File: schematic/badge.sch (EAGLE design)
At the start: 13 parts, among them IC1 4051D, IC2 4051D

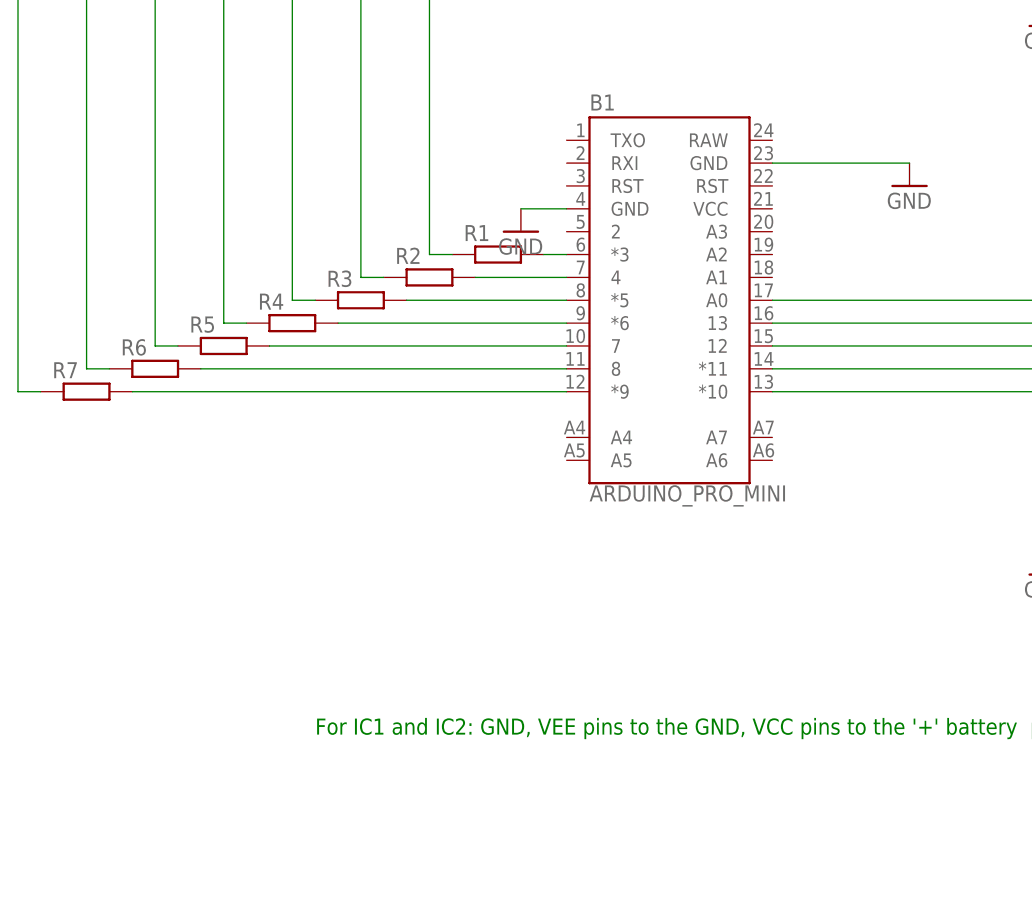
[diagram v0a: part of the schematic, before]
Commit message: Added schematic
This is first version of the schematic which I used for testing idea and
program. Now I work for the new design
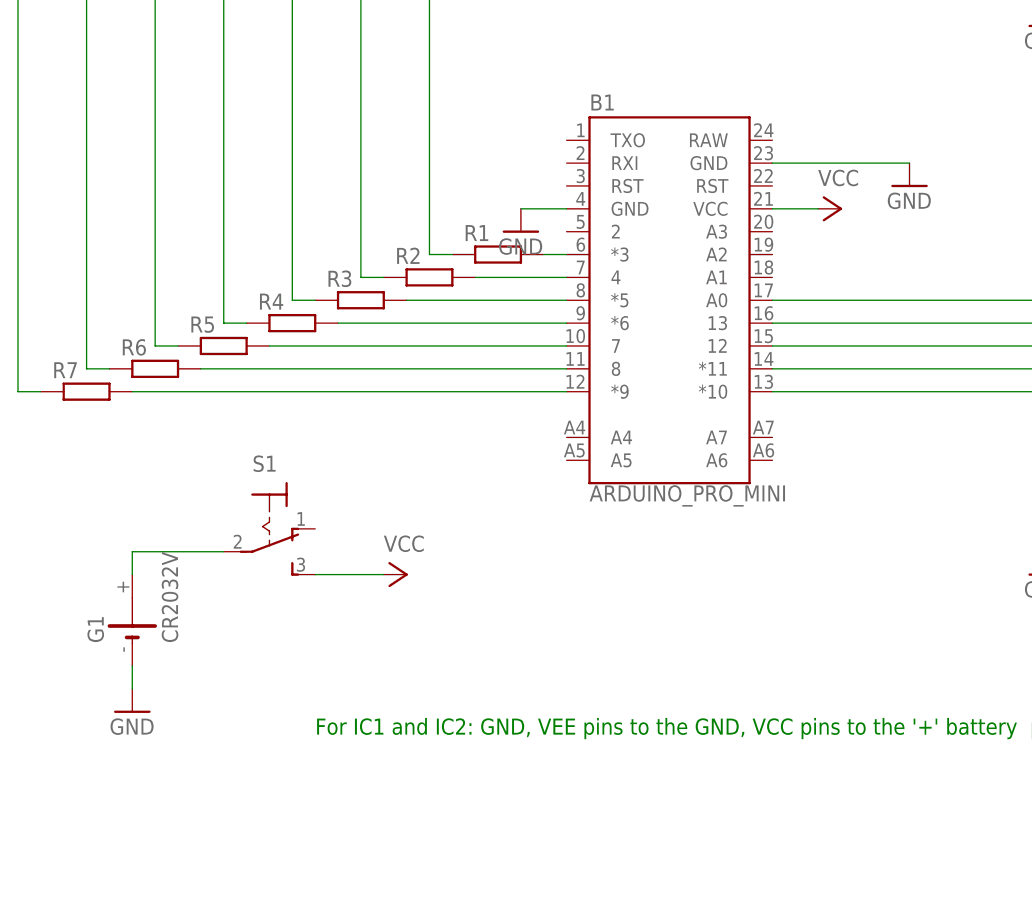
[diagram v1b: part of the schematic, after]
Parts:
- added G1: CR2032V, battery:CR2032V
- added S1: (no value), switch:320-916
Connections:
- new net N$33: G1.+, S1.P
- new net VCC: B1.VCC, S1.S
- net GND: now also G1.-
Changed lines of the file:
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@@
 <part name="GND3" library="supply1" library_urn="urn:adsk.eagle:library:371" deviceset="GND" device=""/>
 <part name="GND4" library="supply1" library_urn="urn:adsk.eagle:library:371" deviceset="GND" device=""/>
+<part name="G1" library="battery" library_urn="urn:adsk.eagle:library:109" deviceset="CR2032V" device="" package3d_urn="urn:adsk.eagle:package:4578/1"/>
+<part name="S1" library="switch" library_urn="urn:adsk.eagle:library:380" deviceset="320-916" device="" package3d_urn="urn:adsk.eagle:package:27678/1"/>
+<part name="P+1" library="supply1" library_urn="urn:adsk.eagle:library:371" deviceset="VCC" device=""/>
+<part name="P+2" library="supply1" library_urn="urn:adsk.eagle:library:371" deviceset="VCC" device=""/>
+<part name="GND5" library="supply1" library_urn="urn:adsk.eagle:library:371" deviceset="GND" device=""/>
 </parts>
 <sheets>
@@
 <instance part="GND3" gate="1" x="15.24" y="43.18"/>
 <instance part="GND4" gate="1" x="-27.94" y="38.1"/>
+<instance part="G1" gate="1" x="-71.12" y="-5.08" rot="R90"/>
+<instance part="S1" gate="1" x="-55.88" y="5.08" rot="R270"/>
+<instance part="P+1" gate="VCC" x="-40.64" y="0" rot="R270"/>
+<instance part="P+2" gate="VCC" x="7.62" y="40.64" rot="R270"/>
+<instance part="GND5" gate="1" x="-71.12" y="-15.24"/>
 </instances>
 <busses>
@@
 <wire x1="-27.94" y1="40.64" x2="-22.86" y2="40.64" width="0.1524" layer="91"/>
 </segment>
+<segment>
+<pinref part="GND5" gate="1" pin="GND"/>
+<pinref part="G1" gate="1" pin="-"/>
+<wire x1="-71.12" y1="-12.7" x2="-71.12" y2="-10.16" width="0.1524" layer="91"/>
+</segment>
 </net>
 <net name="N$8" class="0">
@@
 </segment>
 </net>
+<net name="VCC" class="0">
+<segment>
+<pinref part="P+2" gate="VCC" pin="VCC"/>
+<pinref part="B1" gate="G$1" pin="VCC"/>
+<wire x1="5.08" y1="40.64" x2="0" y2="40.64" width="0.1524" layer="91"/>
+</segment>
+<segment>
+<pinref part="P+1" gate="VCC" pin="VCC"/>
+<pinref part="S1" gate="1" pin="S"/>
+<wire x1="-43.18" y1="0" x2="-50.8" y2="0" width="0.1524" layer="91"/>
+</segment>
+</net>
+<net name="N$33" class="0">
+<segment>
+<pinref part="S1" gate="1" pin="P"/>
+<wire x1="-60.96" y1="2.54" x2="-71.12" y2="2.54" width="0.1524" layer="91"/>
+<pinref part="G1" gate="1" pin="+"/>
+<wire x1="-71.12" y1="2.54" x2="-71.12" y2="0" width="0.1524" layer="91"/>
+</segment>
+</net>

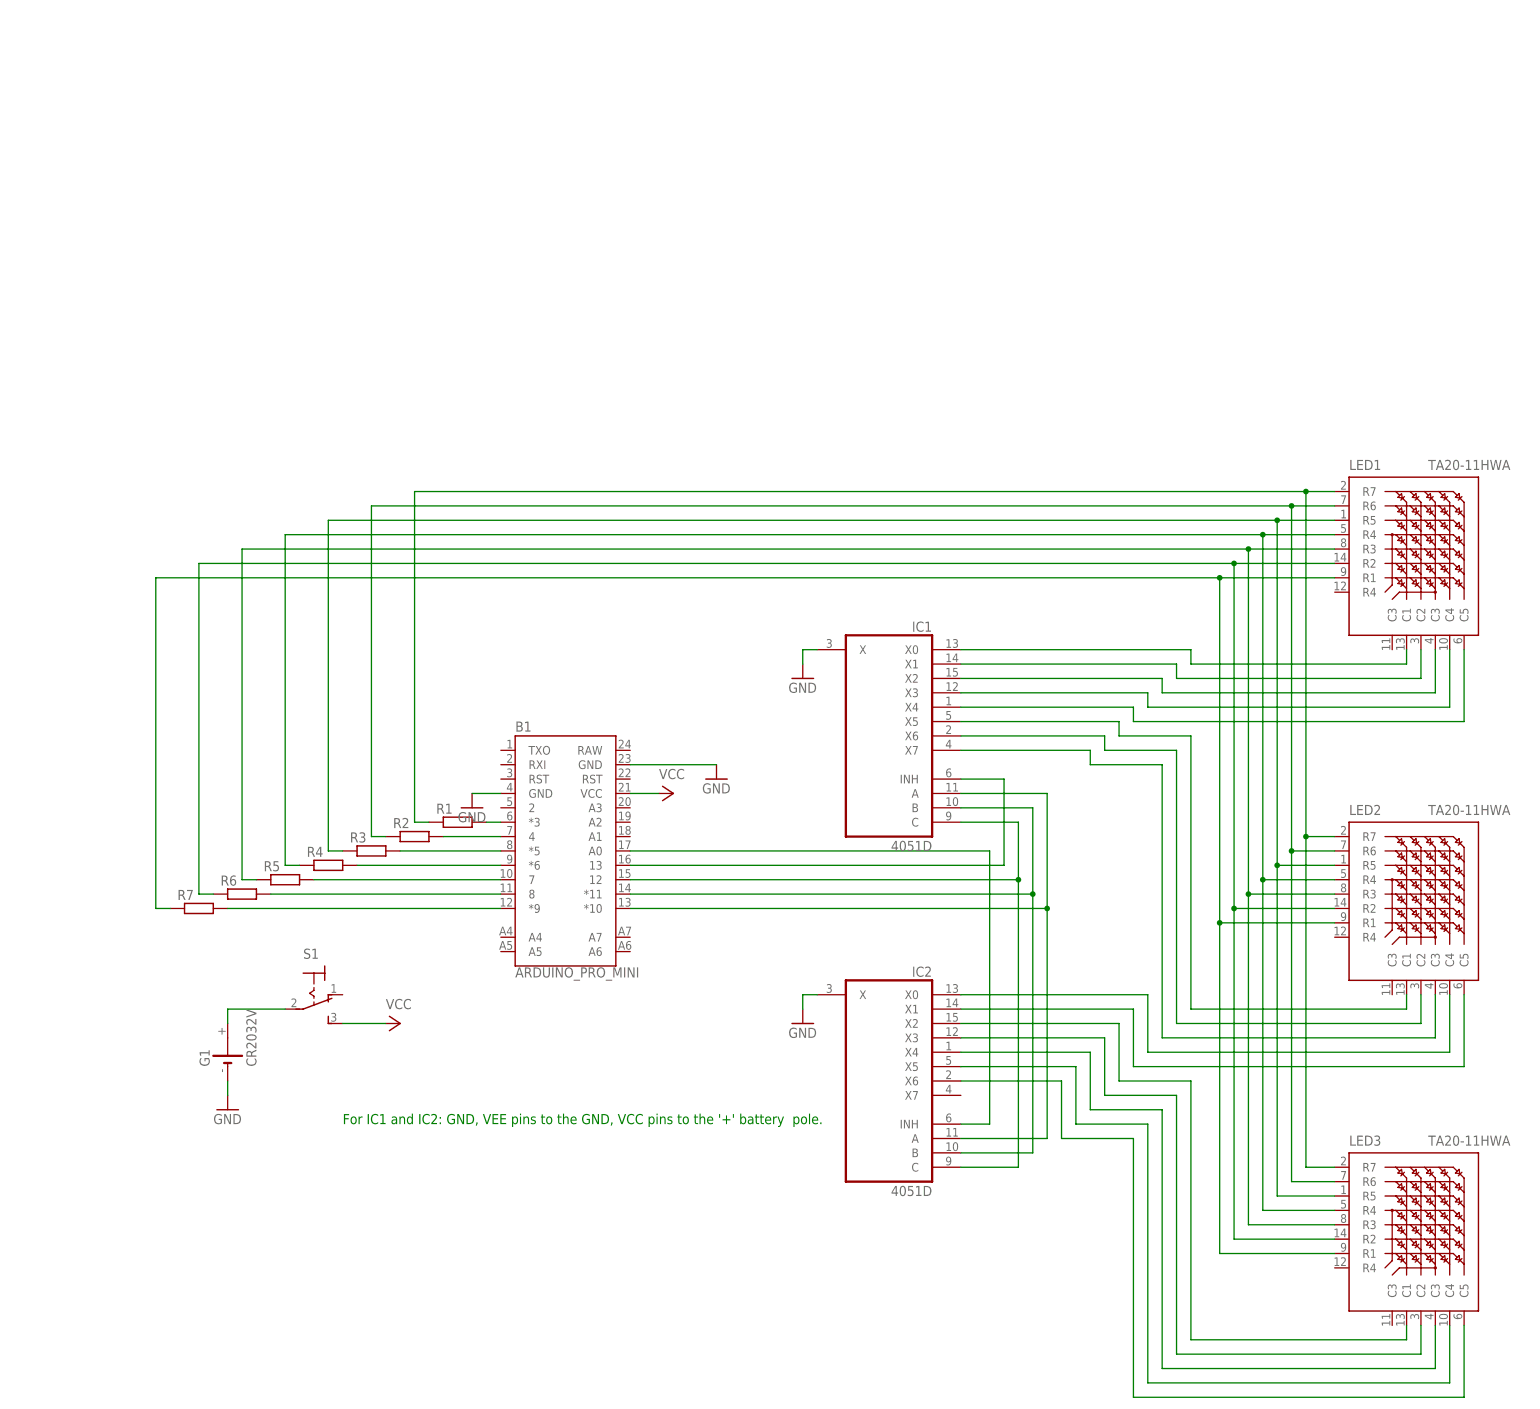
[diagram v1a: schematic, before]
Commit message: Added transistors for increasing LEDs current
Using p-channel FETs for supplying LEDs
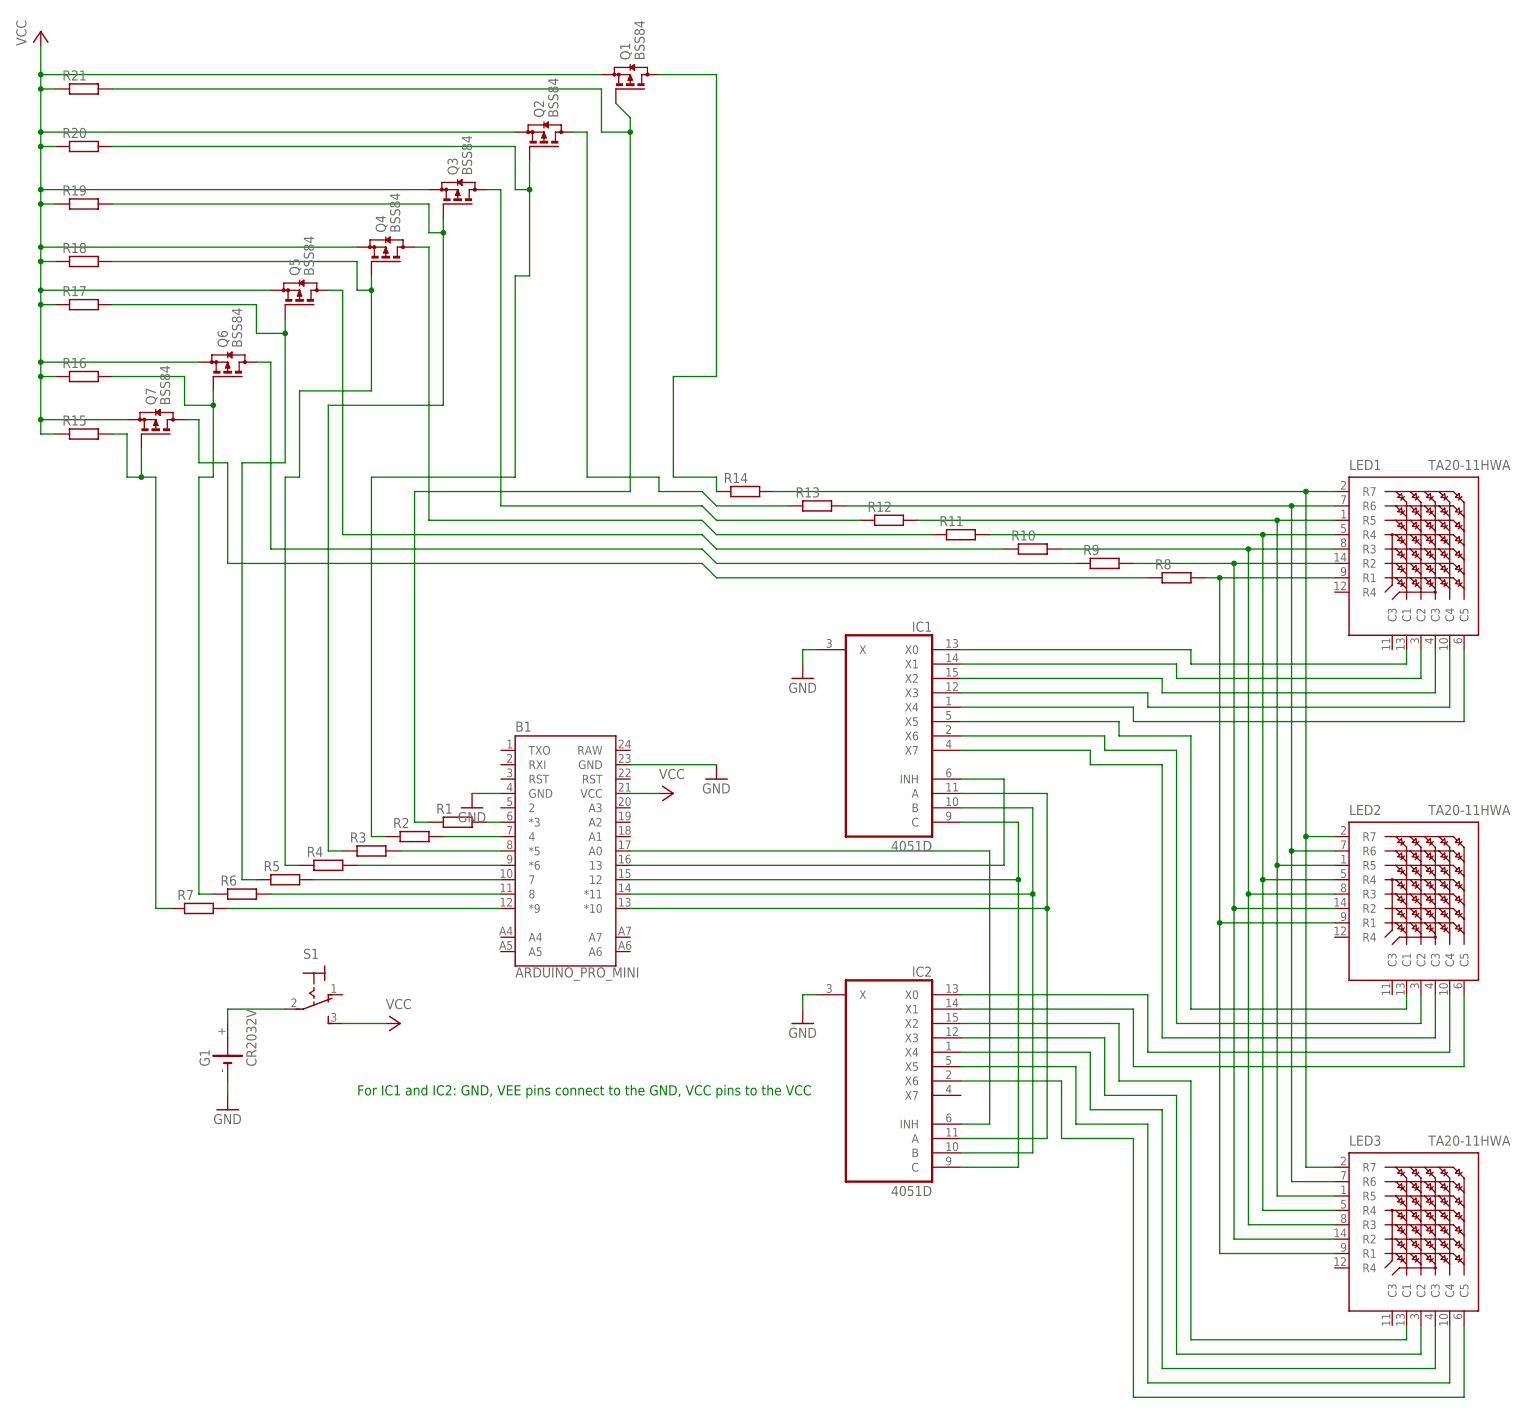
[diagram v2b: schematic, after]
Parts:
- added Q1, Q2, Q3, Q4, Q5, Q6, Q7: BSS84, transistor-small-signal:BSS84
- added R10, R11, R12, R13, R14, R8, R9: (no value), resistor:R-EU_R0805
- added R15, R16, R17, R18, R19, R20, R21: (no value), resistor:R-EU_R0603
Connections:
- new net N$34: Q7.G, R15.2, R7.1
- new net N$35: Q6.G, R16.2, R6.1
- new net N$38: Q5.G, R17.2, R5.1
- new net N$39: Q3.G, R19.2, R3.1
- new net N$40: Q4.G, R18.2, R4.1
- new net N$41: Q2.G, R2.1, R20.2
- new net N$42: Q1.G, R1.1, R21.2
- new net N$43: Q3.D, R12.1
- new net N$44: Q7.D, R8.1
- new net N$45: Q6.D, R9.1
- new net N$46: Q5.D, R10.1
- new net N$47: Q4.D, R11.1
- new net N$48: Q2.D, R13.1
- new net N$49: Q1.D, R14.1
- net N$1: now also R14.2; no longer R1.1
- net N$2: now also R13.2; no longer R2.1
- net N$3: now also R12.2; no longer R3.1
- net N$4: now also R11.2; no longer R4.1
- net N$5: now also R10.2; no longer R5.1
- net N$6: now also R9.2; no longer R6.1
- net N$7: now also R8.2; no longer R7.1
- net VCC: now also Q1.S, Q2.S, Q3.S, Q4.S, Q5.S, Q6.S, Q7.S, R15.1, R16.1, R17.1, R18.1, R19.1, R20.1, R21.1
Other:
- note added: "For IC1 and IC2: GND, VEE pins connect to the GND, VCC pins to the VCC"
- note removed: "For IC1 and IC2: GND, VEE pins to the GND, VCC pins to the '+' battery pole."
